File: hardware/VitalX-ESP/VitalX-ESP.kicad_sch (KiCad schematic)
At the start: 56 parts, among them J1 ECG Probe connector, J2 GSR Probe connector, J3 UART, J4 JTAG, J5 Power terminal, Q1 BSS138, SW2 Reset, U1 AD8232ACPZ-R7, U3 ADP160AUJZ-1.8-R7, U4 ADPD144RI-ACEZ-RL, U5 AMS1117-3.3, U6 MCP601-xOT, U7 ESP32-S2-WROOM

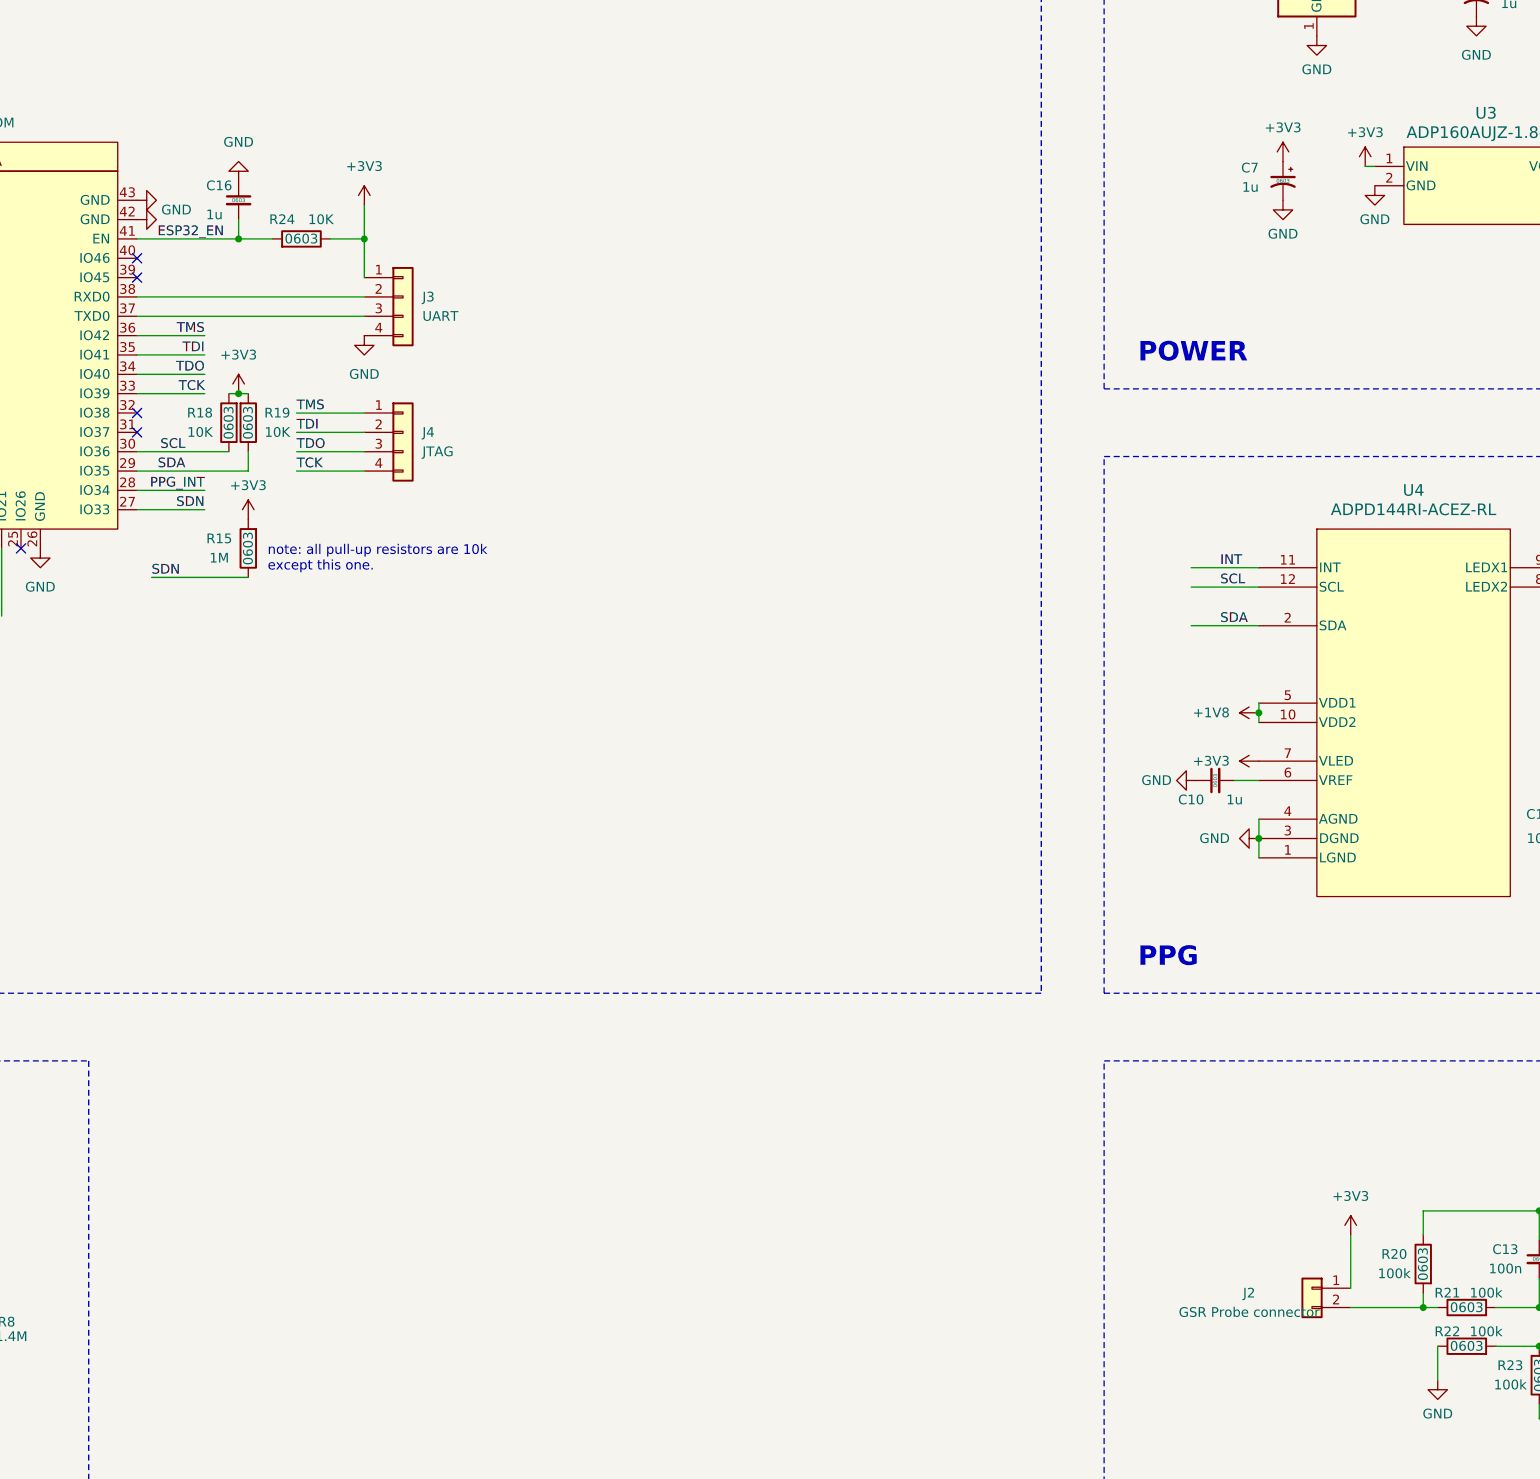
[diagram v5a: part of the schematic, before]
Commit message: [nightly] Program/Debug interface.
Implementing proper program connector (2x3) and jtag (2x5)
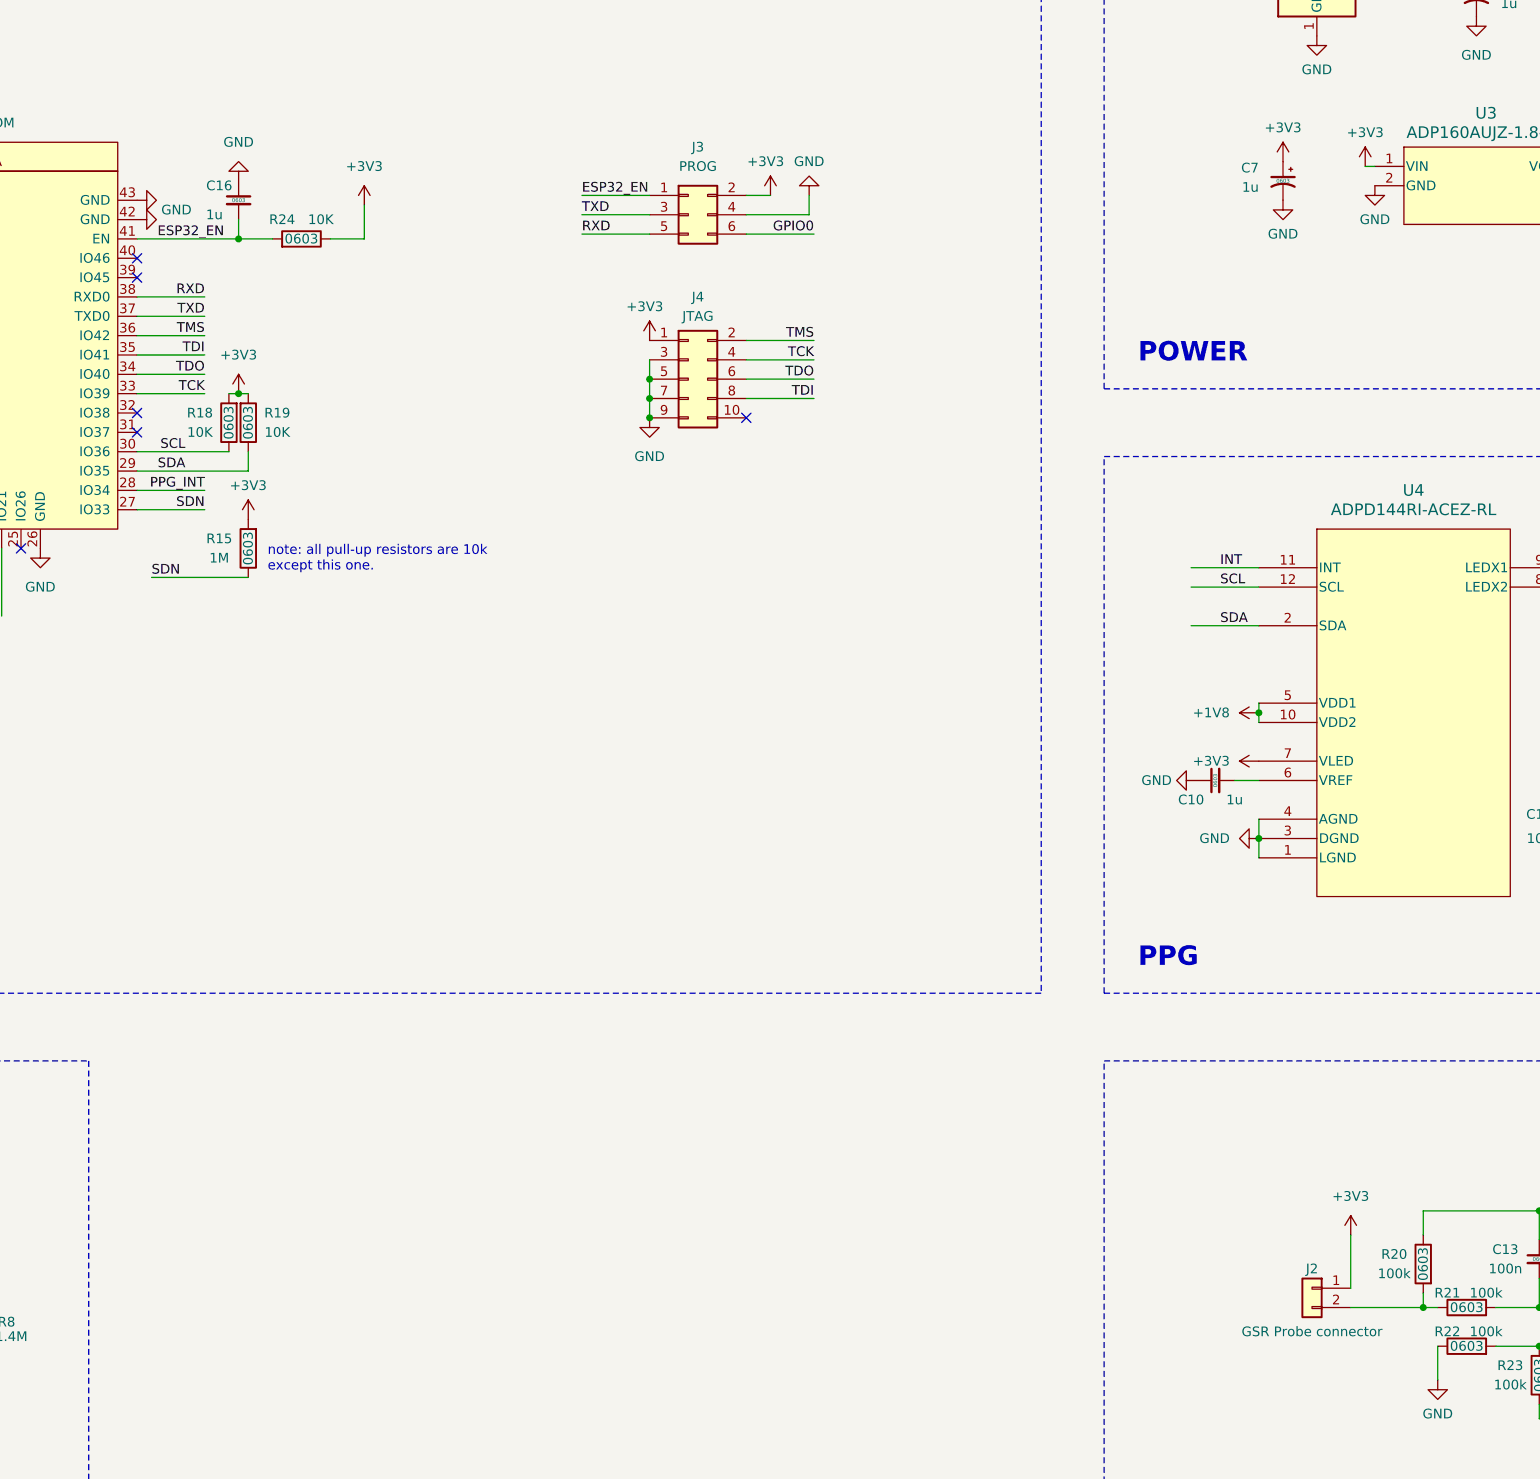
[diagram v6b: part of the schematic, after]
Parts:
- removed J3: UART, Connector_PinHeader_2.54mm:PinHeader_1x04_P2.54mm_Vertical_SMD_Pin1Left, symbol Connector_Generic:Conn_01x04
- removed J4: JTAG, Connector_PinHeader_2.54mm:PinHeader_1x04_P2.54mm_Vertical_SMD_Pin1Left, symbol Connector_Generic:Conn_01x04
- added J3: PROG, Connector_PinHeader_2.54mm:PinHeader_2x03_P2.54mm_Vertical, symbol Connector_Generic:Conn_02x03_Odd_Even
- added J4: JTAG, Connector_PinHeader_2.54mm:PinHeader_2x05_P2.54mm_Vertical, symbol Connector_Generic:Conn_02x05_Odd_Even
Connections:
- net +3V3: now also J3.2 (Pin_2), J4.1 (Pin_1)
- net ESP32_EN: now also J3.1 (Pin_1)
- net GND: now also J3.4 (Pin_4), J4.3 (Pin_3), J4.5 (Pin_5), J4.7 (Pin_7), J4.9 (Pin_9)
- net GPIO0: now also J3.6 (Pin_6)
- net TCK: now also J4.4 (Pin_4)
- net TDI: now also J4.8 (Pin_8)
- net TDO: now also J4.6 (Pin_6)
- net TMS: now also J4.2 (Pin_2)
- net TXD: now reaches U7.37 (TXD0)
- net TXD: now also J3.3 (Pin_3)
- net RXD: now reaches U7.38 (RXD0)
- net RXD: now also J3.5 (Pin_5)
- no-connect marks 23 -> 24

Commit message: [nightly] Various footprint update.
Change footprints:
- Reset button
- GSR conn header
Minor PCB changes:
- Increase thermal relief via size
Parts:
- added R26: 0, Resistor_SMD:R_0603_1608Metric, symbol Device:R
- J2: footprint Connector_PinHeader_2.54mm:PinHeader_1x02_P2.54mm_Vertical_SMD_Pin1Left -> Connector_PinHeader_2.54mm:PinHeader_1x02_P2.54mm_Vertical
- SW2: footprint Button_Switch_THT:SW_PUSH_1P1T_6x3.5mm_H5.0_APEM_MJTP1250 -> Button_Switch_SMD:SW_Tactile_SPST_NO_Straight_CK_PTS636Sx25SMTRLFS
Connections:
- net at R6.2, R7.2: now also R26.2; no longer R8.1
- new net: R26.1, R8.1
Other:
- moved on the sheet: R8
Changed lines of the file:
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@@
     (stroke (width 0) (type default))
   )
-  (wire (pts (xy 149.225 213.995) (xy 149.225 213.36))
-    (stroke (width 0) (type default))
-  )
   (wire (pts (xy 132.715 244.475) (xy 141.605 244.475))
     (stroke (width 0) (type default))
@@
     (stroke (width 0) (type default))
   )
-  (wire (pts (xy 144.78 203.835) (xy 149.225 203.835))
+  (wire (pts (xy 144.78 203.835) (xy 156.845 203.835))
     (stroke (width 0) (type default))
   )
@@
     (stroke (width 0) (type default))
   )
-  (wire (pts (xy 149.225 203.835) (xy 149.225 205.74))
-    (stroke (width 0) (type default))
-  )
   (wire (pts (xy 169.545 74.295) (xy 178.435 74.295))
     (stroke (width 0) (type default))
@@
     (stroke (width 0) (type default))
   )
+  (wire (pts (xy 156.845 203.835) (xy 156.845 205.74))
+    (stroke (width 0) (type default))
+  )
   (wire (pts (xy 144.145 116.205) (xy 144.145 107.315))
     (stroke (width 0) (type default))
@@
     (stroke (width 0) (type default))
   )
+  (wire (pts (xy 156.845 213.36) (xy 156.845 213.995))
+    (stroke (width 0) (type default))
+  )
   (wire (pts (xy 375.92 32.385) (xy 375.92 36.195))
     (stroke (width 0) (type default))
@@
       (effects (font (size 1.27 1.27)))
     )
-    (property "Footprint" "Button_Switch_THT:SW_PUSH_1P1T_6x3.5mm_H5.0_APEM_MJTP1250" (at 88.9 104.775 0)
+    (property "Footprint" "Button_Switch_SMD:SW_Tactile_SPST_NO_Straight_CK_PTS636Sx25SMTRLFS" (at 88.9 104.775 0)
       (effects (font (size 1.27 1.27)) hide)
     )
@@
     )
   )
+  (symbol (lib_id "Device:R") (at 153.035 213.995 270) (unit 1)
+    (in_bom yes) (on_board yes) (dnp no)
+    (property "Reference" "R26" (at 153.035 211.455 90)
+      (effects (font (size 1.27 1.27)))
+    )
+    (property "Value" "0" (at 153.035 216.535 90)
+      (effects (font (size 1.27 1.27)))
+    )
+    (property "Footprint" "Resistor_SMD:R_0603_1608Metric" (at 153.035 212.217 90)
+      (effects (font (size 1.27 1.27)) hide)
+    )
+    (property "Datasheet" "~" (at 153.035 213.995 0)
+      (effects (font (size 1.27 1.27)) hide)
+    )
+    (property "Size" "0603" (at 153.035 213.995 90)
+      (effects (font (size 1.27 1.27)))
+    )
+    (property "description" "resistor" (at 153.035 213.995 0)
+      (effects (font (size 1.27 1.27)) hide)
+    )
+    (property "mouser mnf num" "" (at 153.035 213.995 0)
+      (effects (font (size 1.27 1.27)) hide)
+    )
+    (property "mnf number" "" (at 153.035 213.995 0)
+      (effects (font (size 1.27 1.27)) hide)
+    )
+    (pin "1")
+    (pin "2")
+    (instances
+      (project "VitalX-ESP"
+        (path "/c6ad7dc7-b487-4ed9-a043-5d3a4b3b13ea"
+          (reference "R26") (unit 1)
+        )
+      )
+    )
+  )
   (symbol (lib_id "power:+5V") (at 384.81 32.385 0) (unit 1)
     (in_bom yes) (on_board yes) (dnp no) (fields_autoplaced)
@@
       (effects (font (size 1.27 1.27)))
     )
-    (property "Footprint" "Connector_PinHeader_2.54mm:PinHeader_1x02_P2.54mm_Vertical_SMD_Pin1Left" (at 323.85 204.47 0)
+    (property "Footprint" "Connector_PinHeader_2.54mm:PinHeader_1x02_P2.54mm_Vertical" (at 323.85 204.47 0)
       (effects (font (size 1.27 1.27)) hide)
     )
@@
     )
   )
-  (symbol (lib_id "Device:R") (at 149.225 209.55 180) (unit 1)
+  (symbol (lib_id "Device:R") (at 156.845 209.55 180) (unit 1)
     (in_bom yes) (on_board yes) (dnp no)
-    (property "Reference" "R8" (at 152.4 208.915 0)
+    (property "Reference" "R8" (at 160.02 208.915 0)
       (effects (font (size 1.27 1.27)))
     )
-    (property "Value" "1.4M" (at 153.035 210.82 0)
+    (property "Value" "1.4M" (at 160.655 210.82 0)
       (effects (font (size 1.27 1.27)))
     )
-    (property "Footprint" "Resistor_SMD:R_0603_1608Metric" (at 151.003 209.55 90)
+    (property "Footprint" "Resistor_SMD:R_0603_1608Metric" (at 158.623 209.55 90)
       (effects (font (size 1.27 1.27)) hide)
     )
-    (property "Datasheet" "~" (at 149.225 209.55 0)
+    (property "Datasheet" "~" (at 156.845 209.55 0)
       (effects (font (size 1.27 1.27)) hide)
     )
-    (property "Size" "0603" (at 149.225 209.55 90)
+    (property "Size" "0603" (at 156.845 209.55 90)
       (effects (font (size 1.27 1.27)))
     )
-    (property "description" "resistor" (at 149.225 209.55 0)
+    (property "description" "resistor" (at 156.845 209.55 0)
       (effects (font (size 1.27 1.27)) hide)
     )
-    (property "mouser mnf num" "" (at 149.225 209.55 0)
+    (property "mouser mnf num" "" (at 156.845 209.55 0)
       (effects (font (size 1.27 1.27)) hide)
     )
-    (property "mnf number" "" (at 149.225 209.55 0)
+    (property "mnf number" "" (at 156.845 209.55 0)
       (effects (font (size 1.27 1.27)) hide)
     )

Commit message: [nightly] Various footprint update.
Footprint changes:
- Boot select SMD -> Through-hole
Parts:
- JP1: footprint Connector_PinHeader_2.54mm:PinHeader_1x02_P2.54mm_Vertical_SMD_Pin1Left -> Connector_PinHeader_2.54mm:PinHeader_1x02_P2.54mm_Vertical
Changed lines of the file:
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@@
       (effects (font (size 1.27 1.27)))
     )
-    (property "Footprint" "Connector_PinHeader_2.54mm:PinHeader_1x02_P2.54mm_Vertical_SMD_Pin1Left" (at 89.535 93.98 0)
+    (property "Footprint" "Connector_PinHeader_2.54mm:PinHeader_1x02_P2.54mm_Vertical" (at 89.535 93.98 0)
       (effects (font (size 1.27 1.27)) hide)
     )
